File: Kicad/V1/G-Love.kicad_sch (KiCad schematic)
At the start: 10 parts

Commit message: remove level shifter from tft
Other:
- note removed: "Mode select inside the wrist"
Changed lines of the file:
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@@
-		)
-	)
-	(text "Mode select inside the wrist\n"
-		(exclude_from_sim no)
-		(at 146.812 136.906 0)
-		(effects
-			(font
-				(size 1.27 1.27)
-			)
 		)
 	)

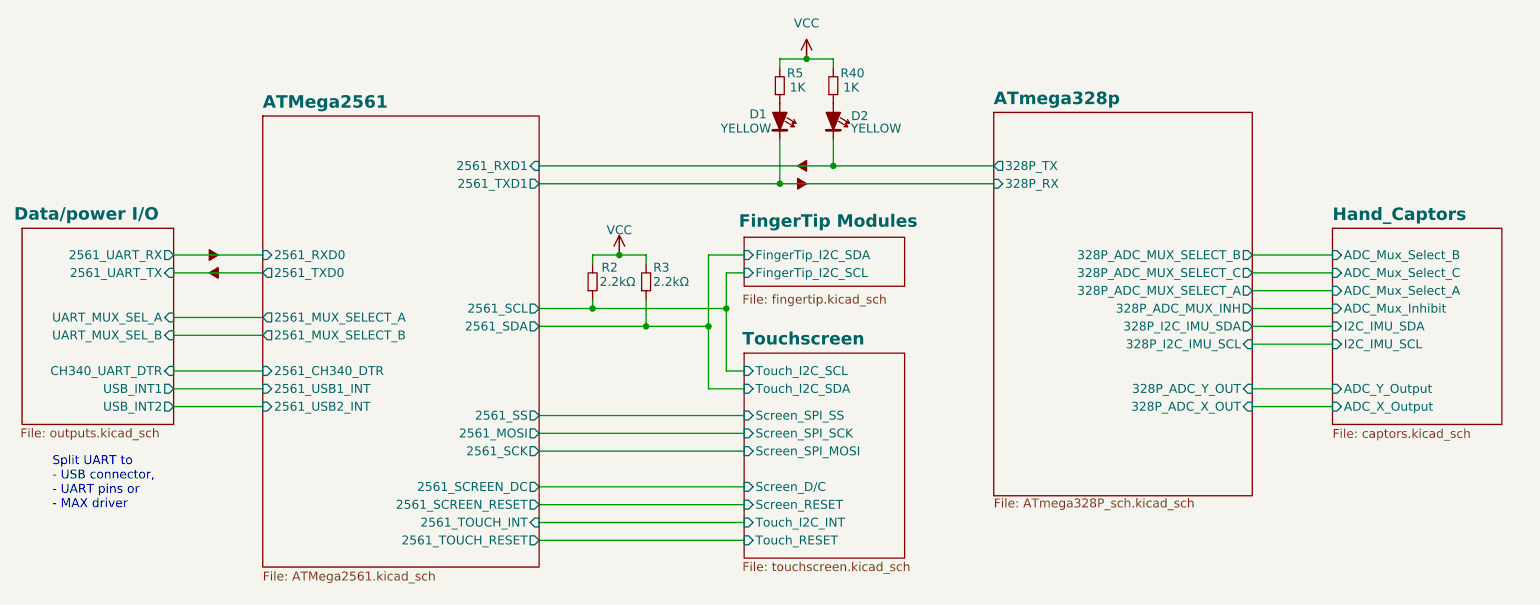
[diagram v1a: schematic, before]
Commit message: ERC almost done, footprint to assign
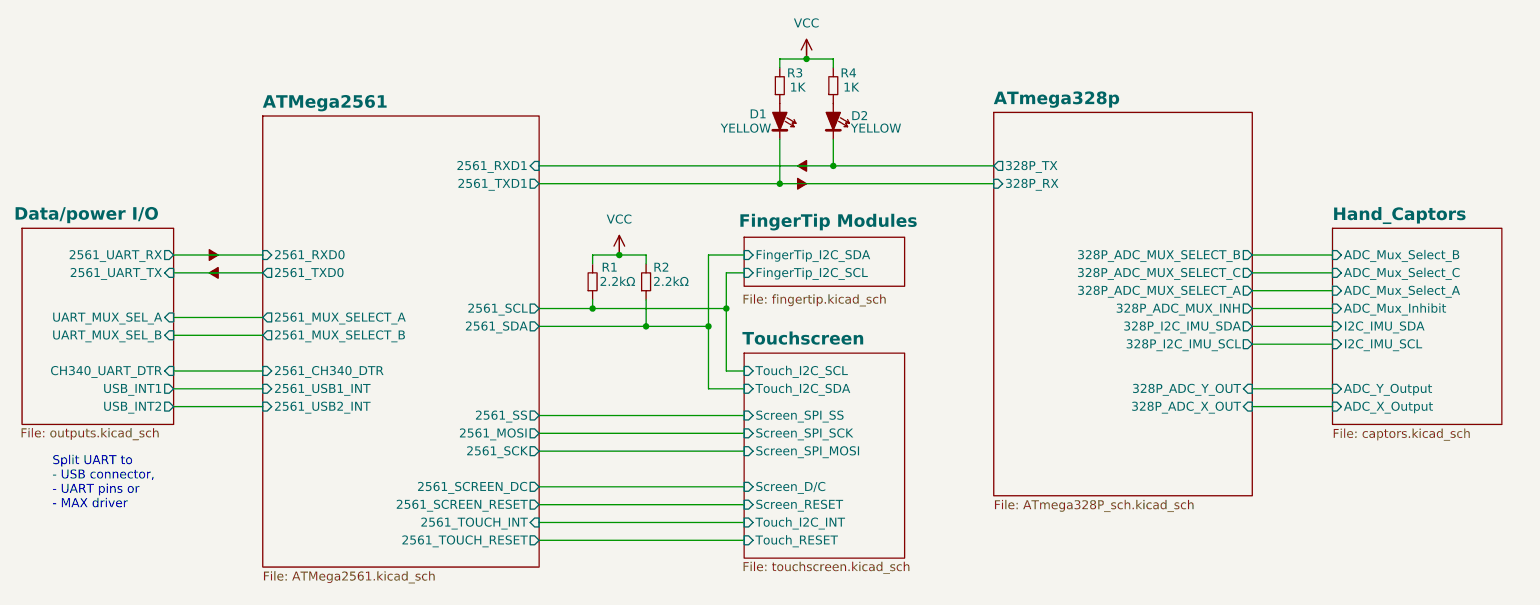
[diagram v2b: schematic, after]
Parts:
- renumbered R2 to R1, R3 to R2, R5 to R3, R40 to R4, flow3 to flow1, flow4 to flow2, flow2 to flow3, flow1 to flow4

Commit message: ERC Check
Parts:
- D1, D2: footprint (none) -> MyGlove:LED
- R3, R4: footprint (none) -> MyGlove:Resistor_0603
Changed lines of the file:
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@@
 			)
 		)
-		(property "Footprint" ""
+		(property "Footprint" "MyGlove:LED"
 			(at 138.43 71.12 0)
 			(hide yes)
@@
 			)
 		)
-		(property "Footprint" ""
+		(property "Footprint" "MyGlove:Resistor_0603"
 			(at 146.05 66.04 0)
 			(hide yes)
@@
 			)
 		)
-		(property "Footprint" ""
+		(property "Footprint" "MyGlove:LED"
 			(at 146.05 71.12 0)
 			(hide yes)
@@
 		(exclude_from_sim no)
 		(in_bom no)
-		(on_board yes)
+		(on_board no)
 		(in_pos_files yes)
 		(dnp no)
@@
 		(exclude_from_sim no)
 		(in_bom no)
-		(on_board yes)
+		(on_board no)
 		(in_pos_files yes)
 		(dnp no)
@@
 		(exclude_from_sim no)
 		(in_bom no)
-		(on_board yes)
+		(on_board no)
 		(in_pos_files yes)
 		(dnp no)
@@
 			)
 		)
-		(property "Footprint" ""
+		(property "Footprint" "MyGlove:Resistor_0603"
 			(at 138.43 66.04 0)
 			(hide yes)
@@
 		(exclude_from_sim no)
 		(in_bom no)
-		(on_board yes)
-		(in_pos_files yes)
-		(dnp no)
+		(on_board no)
+		(in_pos_files yes)
+		(dnp no)
